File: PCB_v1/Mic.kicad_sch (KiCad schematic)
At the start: 10 parts, among them IC1 MIC_I2S_SPH0645, IC2 MIC_I2S_SPH0645

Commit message: adding the parts library
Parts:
- C1: renamed from C28; footprint 0603-NO -> Capacitor_SMD:C_0805_2012Metric
- C2: renamed from C29; footprint 0603-NO -> Capacitor_SMD:C_0805_2012Metric
- C3: renamed from C30; footprint 0603-NO -> Capacitor_SMD:C_0805_2012Metric
- C4: renamed from C31; footprint 0603-NO -> Capacitor_SMD:C_0805_2012Metric
- R1: renamed from R33; footprint 0603-NO -> Resistor_SMD:R_0805_2012Metric
- R2: renamed from R34; footprint 0603-NO -> Resistor_SMD:R_0805_2012Metric
- R3: renamed from R35; footprint 0603-NO -> Resistor_SMD:R_0805_2012Metric
- R4: renamed from R36; footprint 0603-NO -> Resistor_SMD:R_0805_2012Metric

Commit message: Last push before PCB
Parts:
- C1, C2, C3, C4: footprint Capacitor_SMD:C_0805_2012Metric -> Adafruit I2S Mic SPK0415HM4H:0805-NO
- IC1, IC2: footprint SPH0645LM4H -> Adafruit I2S Mic SPK0415HM4H:SPH0645LM4H
- R1, R2, R3, R4: footprint Resistor_SMD:R_0805_2012Metric -> Adafruit I2S Mic SPK0415HM4H:0603-NO
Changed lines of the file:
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@@
 			)
 		)
-		(property "Footprint" "Capacitor_SMD:C_0805_2012Metric"
+		(property "Footprint" "Adafruit I2S Mic SPK0415HM4H:0805-NO"
 			(at 119.38 74.93 0)
 			(effects
@@
 			)
 		)
-		(property "Footprint" "Resistor_SMD:R_0805_2012Metric"
+		(property "Footprint" "Adafruit I2S Mic SPK0415HM4H:0603-NO"
 			(at 138.43 116.84 0)
 			(effects
@@
 			)
 		)
-		(property "Footprint" "Resistor_SMD:R_0805_2012Metric"
+		(property "Footprint" "Adafruit I2S Mic SPK0415HM4H:0603-NO"
 			(at 189.23 115.57 0)
 			(effects
@@
 			)
 		)
-		(property "Footprint" "SPH0645LM4H"
+		(property "Footprint" "Adafruit I2S Mic SPK0415HM4H:SPH0645LM4H"
 			(at 173.99 121.92 0)
 			(effects
@@
 			)
 		)
-		(property "Footprint" "Capacitor_SMD:C_0805_2012Metric"
+		(property "Footprint" "Adafruit I2S Mic SPK0415HM4H:0805-NO"
 			(at 120.65 123.19 0)
 			(effects
@@
 			)
 		)
-		(property "Footprint" "Resistor_SMD:R_0805_2012Metric"
+		(property "Footprint" "Adafruit I2S Mic SPK0415HM4H:0603-NO"
 			(at 189.23 64.77 0)
 			(effects
@@
 			)
 		)
-		(property "Footprint" "Resistor_SMD:R_0805_2012Metric"
+		(property "Footprint" "Adafruit I2S Mic SPK0415HM4H:0603-NO"
 			(at 138.43 77.47 0)
 			(effects
@@
 			)
 		)
-		(property "Footprint" "SPH0645LM4H"
+		(property "Footprint" "Adafruit I2S Mic SPK0415HM4H:SPH0645LM4H"
 			(at 172.72 72.39 0)
 			(effects
@@
 			)
 		)
-		(property "Footprint" "Capacitor_SMD:C_0805_2012Metric"
+		(property "Footprint" "Adafruit I2S Mic SPK0415HM4H:0805-NO"
 			(at 129.54 74.93 0)
 			(effects
@@
 			)
 		)
-		(property "Footprint" "Capacitor_SMD:C_0805_2012Metric"
+		(property "Footprint" "Adafruit I2S Mic SPK0415HM4H:0805-NO"
 			(at 130.81 123.19 0)
 			(effects

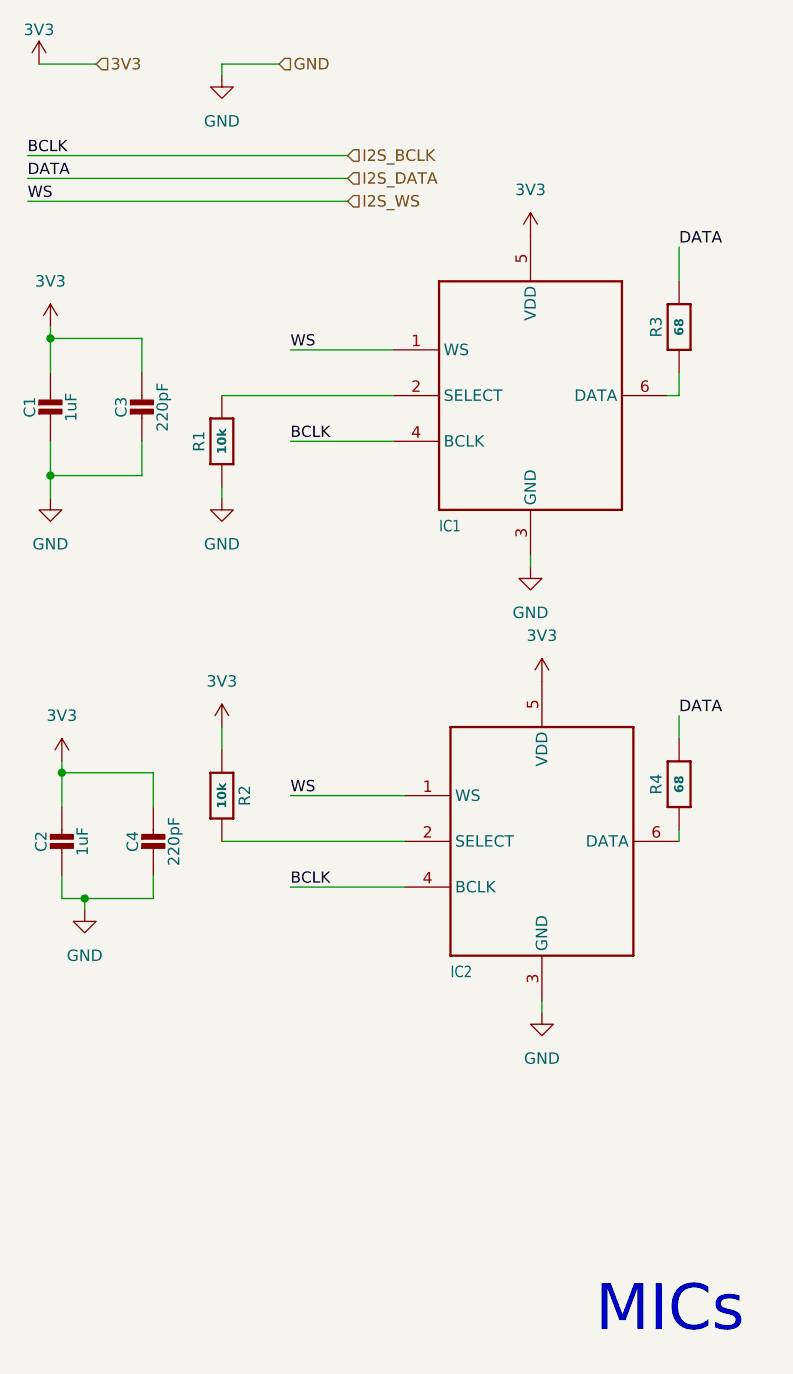
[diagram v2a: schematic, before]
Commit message: changed the MICs to JST headers
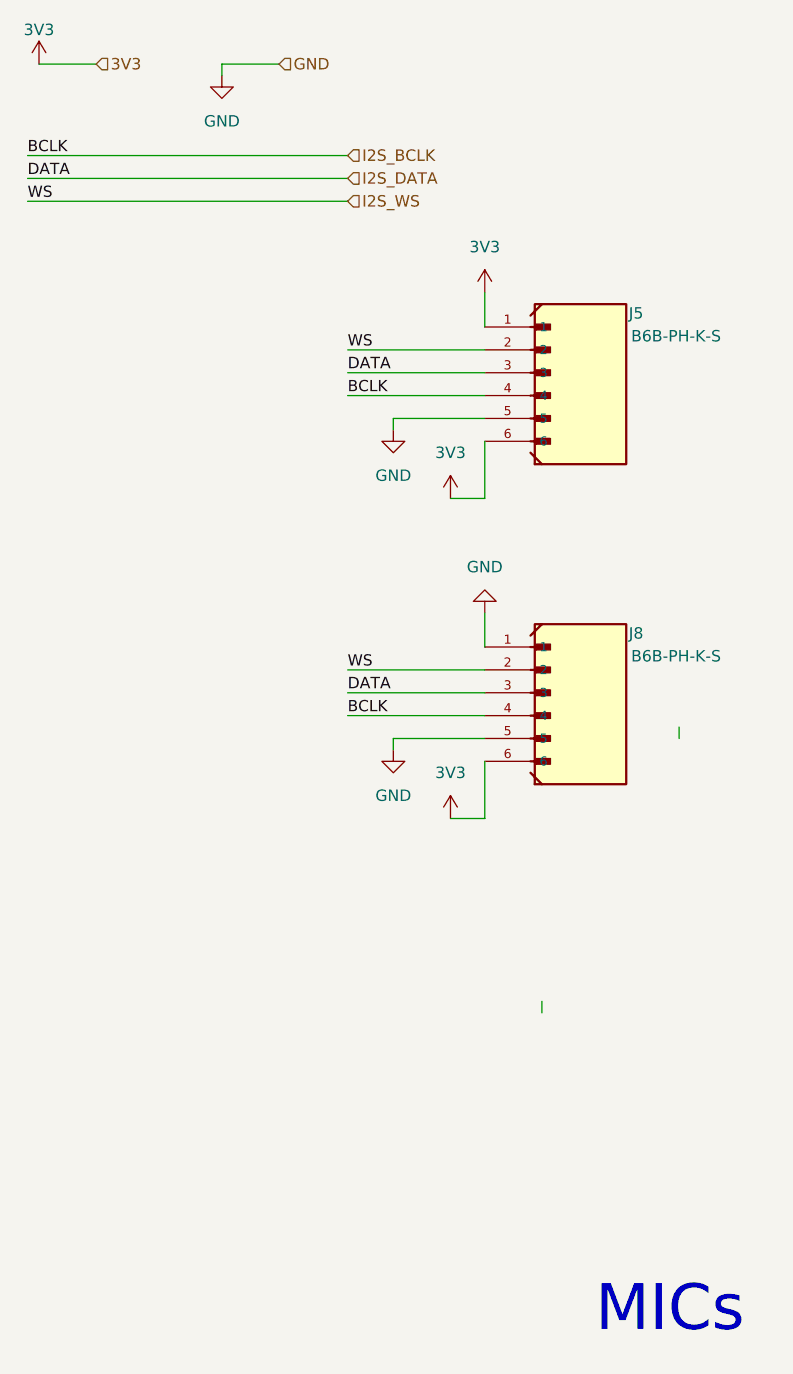
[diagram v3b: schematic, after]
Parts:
- removed C1, C2: 1uF, Adafruit I2S Mic SPK0415HM4H:0805-NO, symbol Adafruit I2S Mic SPK0415HM4H-eagle-import:CAP_CERAMIC0805-NOOUTLINE
- removed C3, C4: 220pF, Adafruit I2S Mic SPK0415HM4H:0805-NO, symbol Adafruit I2S Mic SPK0415HM4H-eagle-import:CAP_CERAMIC0805-NOOUTLINE
- removed IC1, IC2: MIC_I2S_SPH0645, Adafruit I2S Mic SPK0415HM4H:SPH0645LM4H, symbol Adafruit I2S Mic SPK0415HM4H-eagle-import:MIC_I2S_SPH0645
- removed R1, R2: 10k, Adafruit I2S Mic SPK0415HM4H:0603-NO, symbol Adafruit I2S Mic SPK0415HM4H-eagle-import:RESISTOR_0603_NOOUT
- removed R3, R4: 68, Adafruit I2S Mic SPK0415HM4H:0603-NO, symbol Adafruit I2S Mic SPK0415HM4H-eagle-import:RESISTOR_0603_NOOUT
- added J5, J8: B6B-PH-K-S, B6B-PH-K-S:JST_B6B-PH-K-S, symbol GT_LIbrary:B6B-PH-K-S
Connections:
- net 3V3: now also J5.1, J5.6, J8.6
- net GND: now also J5.5, J8.1, J8.5
- net I2S_BCLK: now also J5.4, J8.4
- net I2S_DATA: now also J5.3, J8.3
- net I2S_WS: now also J5.2, J8.2

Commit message: Update before adding AGND for the power delivery
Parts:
- renumbered J5 to J2, J8 to J3
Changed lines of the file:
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@@
 		(dnp no)
 		(fields_autoplaced yes)
-		(property "Reference" "#PWR024"
+		(property "Reference" "#PWR018"
 			(at 157.48 82.55 0)
 			(effects
@@
 			(project "tuner time"
 				(path "/353cef6a-fb6e-40d9-89f8-eb54b7aa5118/79104164-7b4e-40bb-8a38-a0ccd20216ef"
-					(reference "#PWR024")
+					(reference "#PWR018")
 					(unit 1)
 				)
@@
 		(dnp no)
 		(fields_autoplaced yes)
-		(property "Reference" "#PWR017"
+		(property "Reference" "#PWR021"
 			(at 163.83 123.19 0)
 			(effects
@@
 			(project "tuner time"
 				(path "/353cef6a-fb6e-40d9-89f8-eb54b7aa5118/79104164-7b4e-40bb-8a38-a0ccd20216ef"
-					(reference "#PWR017")
+					(reference "#PWR021")
 					(unit 1)
 				)
@@
 		(dnp no)
 		(fields_autoplaced yes)
-		(property "Reference" "#PWR018"
+		(property "Reference" "#PWR023"
 			(at 167.64 90.17 0)
 			(effects
@@
 			(project "tuner time"
 				(path "/353cef6a-fb6e-40d9-89f8-eb54b7aa5118/79104164-7b4e-40bb-8a38-a0ccd20216ef"
-					(reference "#PWR018")
+					(reference "#PWR023")
 					(unit 1)
 				)
@@
 		(dnp no)
 		(fields_autoplaced yes)
-		(property "Reference" "#PWR010"
+		(property "Reference" "#PWR019"
 			(at 157.48 118.11 0)
 			(effects
@@
 			(project "tuner time"
 				(path "/353cef6a-fb6e-40d9-89f8-eb54b7aa5118/79104164-7b4e-40bb-8a38-a0ccd20216ef"
-					(reference "#PWR010")
+					(reference "#PWR019")
 					(unit 1)
 				)
@@
 		(dnp no)
 		(fields_autoplaced yes)
-		(property "Reference" "#PWR020"
+		(property "Reference" "#PWR017"
 			(at 138.43 43.18 0)
 			(effects
@@
 			(project "tuner time"
 				(path "/353cef6a-fb6e-40d9-89f8-eb54b7aa5118/79104164-7b4e-40bb-8a38-a0ccd20216ef"
-					(reference "#PWR020")
+					(reference "#PWR017")
 					(unit 1)
 				)
@@
 		(on_board yes)
 		(dnp no)
-		(property "Reference" "#PWR015"
+		(property "Reference" "#PWR016"
 			(at 118.11 39.37 0)
 			(effects
@@
 			(project "tuner time"
 				(path "/353cef6a-fb6e-40d9-89f8-eb54b7aa5118/79104164-7b4e-40bb-8a38-a0ccd20216ef"
-					(reference "#PWR015")
+					(reference "#PWR016")
 					(unit 1)
 				)
@@
 		(dnp no)
 		(fields_autoplaced yes)
-		(property "Reference" "#PWR023"
+		(property "Reference" "#PWR020"
 			(at 163.83 87.63 0)
 			(effects
@@
 			(project "tuner time"
 				(path "/353cef6a-fb6e-40d9-89f8-eb54b7aa5118/79104164-7b4e-40bb-8a38-a0ccd20216ef"
-					(reference "#PWR023")
+					(reference "#PWR020")
 					(unit 1)
 				)
@@
 		(on_board yes)
 		(dnp no)
-		(property "Reference" "J5"
+		(property "Reference" "J2"
 			(at 183.642 63.246 0)
 			(effects
@@
 			(project ""
 				(path "/353cef6a-fb6e-40d9-89f8-eb54b7aa5118/79104164-7b4e-40bb-8a38-a0ccd20216ef"
-					(reference "J5")
+					(reference "J2")
 					(unit 1)
 				)
@@
 		(on_board yes)
 		(dnp no)
-		(property "Reference" "J8"
+		(property "Reference" "J3"
 			(at 183.642 98.806 0)
 			(effects
@@
 			(project "tuner time"
 				(path "/353cef6a-fb6e-40d9-89f8-eb54b7aa5118/79104164-7b4e-40bb-8a38-a0ccd20216ef"
-					(reference "J8")
+					(reference "J3")
 					(unit 1)
 				)
@@
 		(dnp no)
 		(fields_autoplaced yes)
-		(property "Reference" "#PWR09"
+		(property "Reference" "#PWR022"
 			(at 167.64 64.77 0)
 			(effects
@@
 			(project "tuner time"
 				(path "/353cef6a-fb6e-40d9-89f8-eb54b7aa5118/79104164-7b4e-40bb-8a38-a0ccd20216ef"
-					(reference "#PWR09")
-					(unit 1)
-				)
+					(reference "#PWR022")
+					(unit 1)
+				)

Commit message: Initial placement draft
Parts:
- J2, J3: footprint B6B-PH-K-S:JST_B6B-PH-K-S -> GT_library:JST_B6B-PH-K-S
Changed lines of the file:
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@@
 		(dnp no)
 		(fields_autoplaced yes)
-		(property "Reference" "#PWR018"
+		(property "Reference" "#PWR025"
 			(at 157.48 82.55 0)
 			(effects
@@
 			(project "tuner time"
 				(path "/353cef6a-fb6e-40d9-89f8-eb54b7aa5118/79104164-7b4e-40bb-8a38-a0ccd20216ef"
-					(reference "#PWR018")
+					(reference "#PWR025")
 					(unit 1)
 				)
@@
 		(dnp no)
 		(fields_autoplaced yes)
-		(property "Reference" "#PWR021"
+		(property "Reference" "#PWR028"
 			(at 163.83 123.19 0)
 			(effects
@@
 			(project "tuner time"
 				(path "/353cef6a-fb6e-40d9-89f8-eb54b7aa5118/79104164-7b4e-40bb-8a38-a0ccd20216ef"
-					(reference "#PWR021")
+					(reference "#PWR028")
 					(unit 1)
 				)
@@
 		(dnp no)
 		(fields_autoplaced yes)
-		(property "Reference" "#PWR023"
+		(property "Reference" "#PWR030"
 			(at 167.64 90.17 0)
 			(effects
@@
 			(project "tuner time"
 				(path "/353cef6a-fb6e-40d9-89f8-eb54b7aa5118/79104164-7b4e-40bb-8a38-a0ccd20216ef"
-					(reference "#PWR023")
+					(reference "#PWR030")
 					(unit 1)
 				)
@@
 		(dnp no)
 		(fields_autoplaced yes)
-		(property "Reference" "#PWR019"
+		(property "Reference" "#PWR026"
 			(at 157.48 118.11 0)
 			(effects
@@
 			(project "tuner time"
 				(path "/353cef6a-fb6e-40d9-89f8-eb54b7aa5118/79104164-7b4e-40bb-8a38-a0ccd20216ef"
-					(reference "#PWR019")
+					(reference "#PWR026")
 					(unit 1)
 				)
@@
 		(dnp no)
 		(fields_autoplaced yes)
-		(property "Reference" "#PWR017"
+		(property "Reference" "#PWR024"
 			(at 138.43 43.18 0)
 			(effects
@@
 			(project "tuner time"
 				(path "/353cef6a-fb6e-40d9-89f8-eb54b7aa5118/79104164-7b4e-40bb-8a38-a0ccd20216ef"
-					(reference "#PWR017")
+					(reference "#PWR024")
 					(unit 1)
 				)
@@
 		(on_board yes)
 		(dnp no)
-		(property "Reference" "#PWR016"
+		(property "Reference" "#PWR023"
 			(at 118.11 39.37 0)
 			(effects
@@
 			(project "tuner time"
 				(path "/353cef6a-fb6e-40d9-89f8-eb54b7aa5118/79104164-7b4e-40bb-8a38-a0ccd20216ef"
-					(reference "#PWR016")
+					(reference "#PWR023")
 					(unit 1)
 				)
@@
 		(dnp no)
 		(fields_autoplaced yes)
-		(property "Reference" "#PWR020"
+		(property "Reference" "#PWR027"
 			(at 163.83 87.63 0)
 			(effects
@@
 			(project "tuner time"
 				(path "/353cef6a-fb6e-40d9-89f8-eb54b7aa5118/79104164-7b4e-40bb-8a38-a0ccd20216ef"
-					(reference "#PWR020")
+					(reference "#PWR027")
 					(unit 1)
 				)
@@
 			)
 		)
-		(property "Footprint" "B6B-PH-K-S:JST_B6B-PH-K-S"
+		(property "Footprint" "GT_library:JST_B6B-PH-K-S"
 			(at 177.8 72.39 0)
 			(effects
@@
 		)
 		(property "SnapEDA_Link" ""
+			(at 177.8 72.39 0)
+			(effects
+				(font
+					(size 1.27 1.27)
+				)
+				(hide yes)
+			)
+		)
+		(property "MFP" ""
 			(at 177.8 72.39 0)
 			(effects
@@
 			)
 		)
-		(property "Footprint" "B6B-PH-K-S:JST_B6B-PH-K-S"
+		(property "Footprint" "GT_library:JST_B6B-PH-K-S"
 			(at 177.8 107.95 0)
 			(effects
@@
 		)
 		(property "SnapEDA_Link" ""
+			(at 177.8 107.95 0)
+			(effects
+				(font
+					(size 1.27 1.27)
+				)
+				(hide yes)
+			)
+		)
+		(property "MFP" ""
 			(at 177.8 107.95 0)
 			(effects
@@
 		(dnp no)
 		(fields_autoplaced yes)
-		(property "Reference" "#PWR022"
+		(property "Reference" "#PWR029"
 			(at 167.64 64.77 0)
 			(effects
@@
 			(project "tuner time"
 				(path "/353cef6a-fb6e-40d9-89f8-eb54b7aa5118/79104164-7b4e-40bb-8a38-a0ccd20216ef"
-					(reference "#PWR022")
-					(unit 1)
-				)
+					(reference "#PWR029")
+					(unit 1)
+				)

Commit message: adjusted placments
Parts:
- renumbered J2 to J1, J3 to J2
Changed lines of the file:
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@@
 		(dnp no)
 		(fields_autoplaced yes)
-		(property "Reference" "#PWR025"
+		(property "Reference" "#PWR028"
 			(at 157.48 82.55 0)
 			(effects
@@
 			(project "tuner time"
 				(path "/353cef6a-fb6e-40d9-89f8-eb54b7aa5118/79104164-7b4e-40bb-8a38-a0ccd20216ef"
-					(reference "#PWR025")
+					(reference "#PWR028")
 					(unit 1)
 				)
@@
 		(dnp no)
 		(fields_autoplaced yes)
-		(property "Reference" "#PWR028"
+		(property "Reference" "#PWR031"
 			(at 163.83 123.19 0)
 			(effects
@@
 			(project "tuner time"
 				(path "/353cef6a-fb6e-40d9-89f8-eb54b7aa5118/79104164-7b4e-40bb-8a38-a0ccd20216ef"
-					(reference "#PWR028")
+					(reference "#PWR031")
 					(unit 1)
 				)
@@
 		(dnp no)
 		(fields_autoplaced yes)
-		(property "Reference" "#PWR030"
+		(property "Reference" "#PWR033"
 			(at 167.64 90.17 0)
 			(effects
@@
 			(project "tuner time"
 				(path "/353cef6a-fb6e-40d9-89f8-eb54b7aa5118/79104164-7b4e-40bb-8a38-a0ccd20216ef"
-					(reference "#PWR030")
+					(reference "#PWR033")
 					(unit 1)
 				)
@@
 		(dnp no)
 		(fields_autoplaced yes)
-		(property "Reference" "#PWR026"
+		(property "Reference" "#PWR029"
 			(at 157.48 118.11 0)
 			(effects
@@
 			(project "tuner time"
 				(path "/353cef6a-fb6e-40d9-89f8-eb54b7aa5118/79104164-7b4e-40bb-8a38-a0ccd20216ef"
-					(reference "#PWR026")
+					(reference "#PWR029")
 					(unit 1)
 				)
@@
 		(dnp no)
 		(fields_autoplaced yes)
-		(property "Reference" "#PWR024"
+		(property "Reference" "#PWR027"
 			(at 138.43 43.18 0)
 			(effects
@@
 			(project "tuner time"
 				(path "/353cef6a-fb6e-40d9-89f8-eb54b7aa5118/79104164-7b4e-40bb-8a38-a0ccd20216ef"
-					(reference "#PWR024")
+					(reference "#PWR027")
 					(unit 1)
 				)
@@
 		(on_board yes)
 		(dnp no)
-		(property "Reference" "#PWR023"
+		(property "Reference" "#PWR026"
 			(at 118.11 39.37 0)
 			(effects
@@
 			(project "tuner time"
 				(path "/353cef6a-fb6e-40d9-89f8-eb54b7aa5118/79104164-7b4e-40bb-8a38-a0ccd20216ef"
-					(reference "#PWR023")
+					(reference "#PWR026")
 					(unit 1)
 				)
@@
 		(dnp no)
 		(fields_autoplaced yes)
-		(property "Reference" "#PWR027"
+		(property "Reference" "#PWR030"
 			(at 163.83 87.63 0)
 			(effects
@@
 			(project "tuner time"
 				(path "/353cef6a-fb6e-40d9-89f8-eb54b7aa5118/79104164-7b4e-40bb-8a38-a0ccd20216ef"
-					(reference "#PWR027")
+					(reference "#PWR030")
 					(unit 1)
 				)
@@
 		(on_board yes)
 		(dnp no)
-		(property "Reference" "J2"
+		(property "Reference" "J1"
 			(at 183.642 63.246 0)
 			(effects
@@
 			(project ""
 				(path "/353cef6a-fb6e-40d9-89f8-eb54b7aa5118/79104164-7b4e-40bb-8a38-a0ccd20216ef"
-					(reference "J2")
+					(reference "J1")
 					(unit 1)
 				)
@@
 		(on_board yes)
 		(dnp no)
-		(property "Reference" "J3"
+		(property "Reference" "J2"
 			(at 183.642 98.806 0)
 			(effects
@@
 			(project "tuner time"
 				(path "/353cef6a-fb6e-40d9-89f8-eb54b7aa5118/79104164-7b4e-40bb-8a38-a0ccd20216ef"
-					(reference "J3")
+					(reference "J2")
 					(unit 1)
 				)
@@
 		(dnp no)
 		(fields_autoplaced yes)
-		(property "Reference" "#PWR029"
+		(property "Reference" "#PWR032"
 			(at 167.64 64.77 0)
 			(effects
@@
 			(project "tuner time"
 				(path "/353cef6a-fb6e-40d9-89f8-eb54b7aa5118/79104164-7b4e-40bb-8a38-a0ccd20216ef"
-					(reference "#PWR029")
-					(unit 1)
-				)
+					(reference "#PWR032")
+					(unit 1)
+				)

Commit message: pushing BOM
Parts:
- J1, J2: MFP (none) -> B6B-PH-K-S
